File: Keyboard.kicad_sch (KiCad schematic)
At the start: 61 parts, among them SW1 SW_Push, SW10 SW_Push, SW11 SW_Push, SW12 SW_Push, SW13 SW_Push, SW14 SW_Push, SW15 SW_Push, SW16 SW_Push, SW17 SW_Push, SW18 SW_Push, SW19 SW_Push, SW2 SW_Push, SW20 SW_Push, SW3 SW_Push, SW4 SW_Push, SW5 SW_Push, SW6 SW_Push, SW7 SW_Push, SW8 SW_Push, SW9 SW_Push, U1 XIAO-nRF52840-SMD, U2 MCP23017_ML

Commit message: One last step before finalizing the KeyPad
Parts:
- SW1, SW10, SW11, SW12, SW13, SW14, SW15, SW16, SW17, SW18, SW19, SW2, SW20, SW3, SW4, SW5, SW6, SW7, SW8, SW9: footprint PCM_marbastlib-xp-choc:SW_choc_v2_HS_CPG135001S30_1u -> PCM_marbastlib-choc:SW_choc_v1_HS_CPG135001S30_1u
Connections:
- net BT_PIN: now also U1.2 (P0.03_A1_D1); no longer U1.1 (P0.02_A0_D0)
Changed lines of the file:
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@@
 	)
 	(no_connect
-		(at 143.51 55.88)
+		(at 143.51 52.07)
 	)
 	(no_connect
@@
 	(global_label "BT_PIN"
 		(shape input)
-		(at 143.51 52.07 180)
+		(at 143.51 55.88 180)
 		(fields_autoplaced yes)
 		(effects
@@
 		)
 		(property "Intersheetrefs" "${INTERSHEET_REFS}"
-			(at 133.6383 52.07 0)
+			(at 133.6383 55.88 0)
 			(effects
 				(font
@@
 			)
 		)
-		(property "Footprint" "PCM_marbastlib-xp-choc:SW_choc_v2_HS_CPG135001S30_1u"
+		(property "Footprint" "PCM_marbastlib-choc:SW_choc_v1_HS_CPG135001S30_1u"
 			(at 69.85 121.92 0)
 			(effects
@@
 			)
 		)
-		(property "Footprint" "PCM_marbastlib-xp-choc:SW_choc_v2_HS_CPG135001S30_1u"
+		(property "Footprint" "PCM_marbastlib-choc:SW_choc_v1_HS_CPG135001S30_1u"
 			(at 107.95 63.5 0)
 			(effects
@@
 			)
 		)
-		(property "Footprint" "PCM_marbastlib-xp-choc:SW_choc_v2_HS_CPG135001S30_1u"
+		(property "Footprint" "PCM_marbastlib-choc:SW_choc_v1_HS_CPG135001S30_1u"
 			(at 52.07 101.6 0)
 			(effects
@@
 			)
 		)
-		(property "Footprint" "PCM_marbastlib-xp-choc:SW_choc_v2_HS_CPG135001S30_1u"
+		(property "Footprint" "PCM_marbastlib-choc:SW_choc_v1_HS_CPG135001S30_1u"
 			(at 69.85 44.45 0)
 			(effects
@@
 			)
 		)
-		(property "Footprint" "PCM_marbastlib-xp-choc:SW_choc_v2_HS_CPG135001S30_1u"
+		(property "Footprint" "PCM_marbastlib-choc:SW_choc_v1_HS_CPG135001S30_1u"
 			(at 69.85 101.6 0)
 			(effects
@@
 			)
 		)
-		(property "Footprint" "PCM_marbastlib-xp-choc:SW_choc_v2_HS_CPG135001S30_1u"
+		(property "Footprint" "PCM_marbastlib-choc:SW_choc_v1_HS_CPG135001S30_1u"
 			(at 69.85 63.5 0)
 			(effects
@@
 			)
 		)
-		(property "Footprint" "PCM_marbastlib-xp-choc:SW_choc_v2_HS_CPG135001S30_1u"
+		(property "Footprint" "PCM_marbastlib-choc:SW_choc_v1_HS_CPG135001S30_1u"
 			(at 52.07 63.5 0)
 			(effects
@@
 			)
 		)
-		(property "Footprint" "PCM_marbastlib-xp-choc:SW_choc_v2_HS_CPG135001S30_1u"
+		(property "Footprint" "PCM_marbastlib-choc:SW_choc_v1_HS_CPG135001S30_1u"
 			(at 69.85 82.55 0)
 			(effects
@@
 			)
 		)
-		(property "Footprint" "PCM_marbastlib-xp-choc:SW_choc_v2_HS_CPG135001S30_1u"
+		(property "Footprint" "PCM_marbastlib-choc:SW_choc_v1_HS_CPG135001S30_1u"
 			(at 52.07 121.92 0)
 			(effects
@@
 			)
 		)
-		(property "Footprint" "PCM_marbastlib-xp-choc:SW_choc_v2_HS_CPG135001S30_1u"
+		(property "Footprint" "PCM_marbastlib-choc:SW_choc_v1_HS_CPG135001S30_1u"
 			(at 107.95 121.92 0)
 			(effects
@@
 			)
 		)
-		(property "Footprint" "PCM_marbastlib-xp-choc:SW_choc_v2_HS_CPG135001S30_1u"
+		(property "Footprint" "PCM_marbastlib-choc:SW_choc_v1_HS_CPG135001S30_1u"
 			(at 88.9 63.5 0)
 			(effects
@@
 			)
 		)
-		(property "Footprint" "PCM_marbastlib-xp-choc:SW_choc_v2_HS_CPG135001S30_1u"
+		(property "Footprint" "PCM_marbastlib-choc:SW_choc_v1_HS_CPG135001S30_1u"
 			(at 88.9 121.92 0)
 			(effects
@@
 			)
 		)
-		(property "Footprint" "PCM_marbastlib-xp-choc:SW_choc_v2_HS_CPG135001S30_1u"
+		(property "Footprint" "PCM_marbastlib-choc:SW_choc_v1_HS_CPG135001S30_1u"
 			(at 88.9 82.55 0)
 			(effects
@@
 			)
 		)
-		(property "Footprint" "PCM_marbastlib-xp-choc:SW_choc_v2_HS_CPG135001S30_1u"
+		(property "Footprint" "PCM_marbastlib-choc:SW_choc_v1_HS_CPG135001S30_1u"
 			(at 88.9 101.6 0)
 			(effects
@@
 			)
 		)
-		(property "Footprint" "PCM_marbastlib-xp-choc:SW_choc_v2_HS_CPG135001S30_1u"
+		(property "Footprint" "PCM_marbastlib-choc:SW_choc_v1_HS_CPG135001S30_1u"
 			(at 88.9 44.45 0)
 			(effects
@@
 			)
 		)
-		(property "Footprint" "PCM_marbastlib-xp-choc:SW_choc_v2_HS_CPG135001S30_1u"
+		(property "Footprint" "PCM_marbastlib-choc:SW_choc_v1_HS_CPG135001S30_1u"
 			(at 52.07 82.55 0)
 			(effects
@@
 			)
 		)
-		(property "Footprint" "PCM_marbastlib-xp-choc:SW_choc_v2_HS_CPG135001S30_1u"
+		(property "Footprint" "PCM_marbastlib-choc:SW_choc_v1_HS_CPG135001S30_1u"
 			(at 107.95 101.6 0)
 			(effects
@@
 			)
 		)
-		(property "Footprint" "PCM_marbastlib-xp-choc:SW_choc_v2_HS_CPG135001S30_1u"
+		(property "Footprint" "PCM_marbastlib-choc:SW_choc_v1_HS_CPG135001S30_1u"
 			(at 107.95 82.55 0)
 			(effects
@@
 			)
 		)
-		(property "Footprint" "PCM_marbastlib-xp-choc:SW_choc_v2_HS_CPG135001S30_1u"
+		(property "Footprint" "PCM_marbastlib-choc:SW_choc_v1_HS_CPG135001S30_1u"
 			(at 107.95 44.45 0)
 			(effects
@@
 			)
 		)
-		(property "Footprint" "PCM_marbastlib-xp-choc:SW_choc_v2_HS_CPG135001S30_1u"
+		(property "Footprint" "PCM_marbastlib-choc:SW_choc_v1_HS_CPG135001S30_1u"
 			(at 52.07 44.45 0)
 			(effects

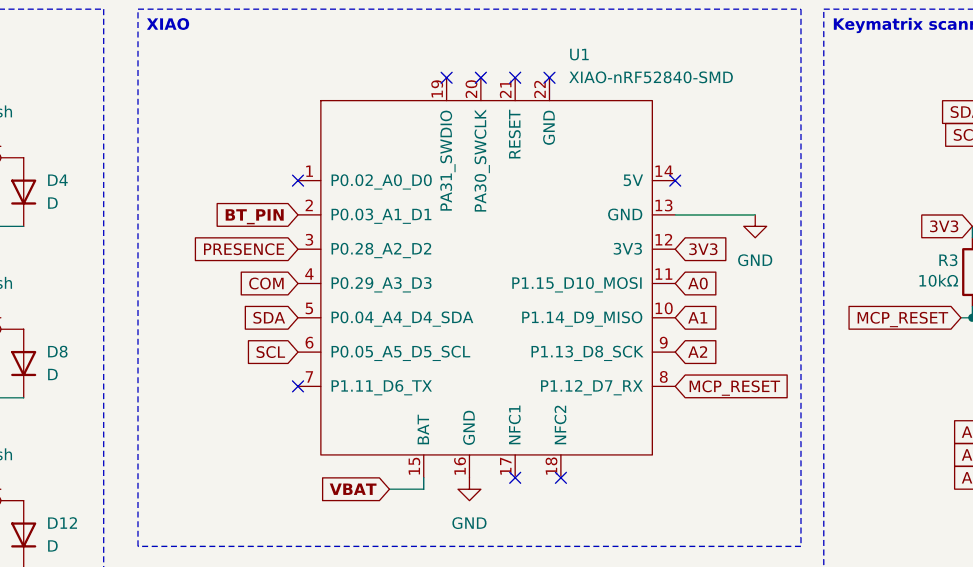
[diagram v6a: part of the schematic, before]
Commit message: Finalized the keypad
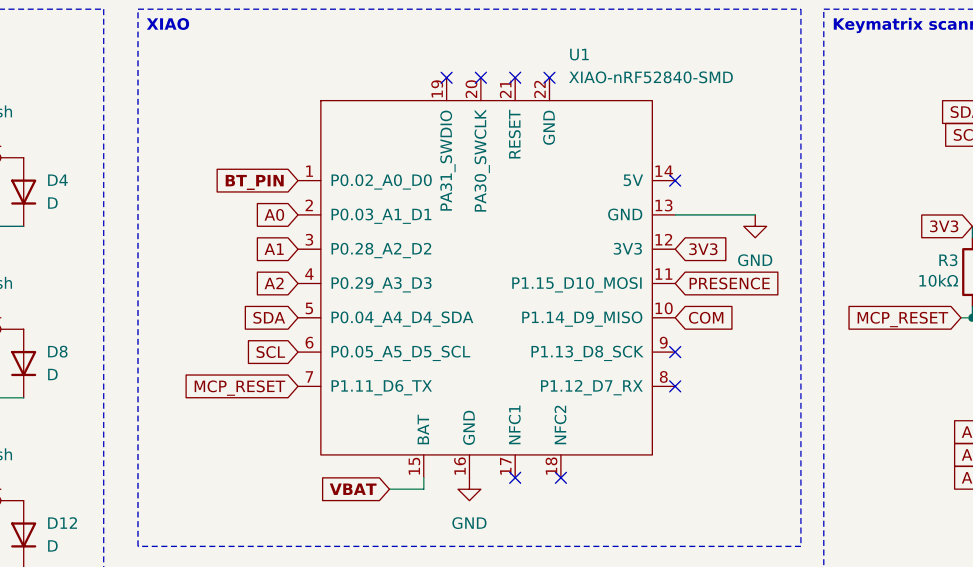
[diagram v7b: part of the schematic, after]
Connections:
- net A0: now also U1.2 (P0.03_A1_D1); no longer U1.11 (P1.15_D10_MOSI)
- net A1: now also U1.3 (P0.28_A2_D2); no longer U1.10 (P1.14_D9_MISO)
- net A2: now also U1.4 (P0.29_A3_D3); no longer U1.9 (P1.13_D8_SCK)
- net BT_PIN: now also U1.1 (P0.02_A0_D0); no longer U1.2 (P0.03_A1_D1)
- net COM: now also U1.10 (P1.14_D9_MISO); no longer U1.4 (P0.29_A3_D3)
- net MCP_RESET: now also U1.7 (P1.11_D6_TX); no longer U1.8 (P1.12_D7_RX)
- net PRESENCE: now also U1.11 (P1.15_D10_MOSI); no longer U1.3 (P0.28_A2_D2)

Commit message: Main board layout
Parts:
- removed D1, D10, D11, D12, D13, D14, D15, D16, D17, D18, D19, D2, D20, D3, D4, D5, D6, D7, D8, D9: D, Diode_SMD:D_SOD-123, symbol Device:D
- removed H1, H2, H3, H4, H5, H6: MountingHole, MountingHole:MountingHole_2.2mm_M2, symbol Mechanical:MountingHole
- removed R1: 806kΩ, Resistor_SMD:R_0805_2012Metric, symbol Device:R
- removed R2: 2MΩ, Resistor_SMD:R_0805_2012Metric, symbol Device:R
- removed R3: 10kΩ, Resistor_SMD:R_0805_2012Metric, symbol Device:R
- removed R4, R5: 4.7kΩ, Resistor_SMD:R_0805_2012Metric, symbol Device:R
- removed SW1, SW10, SW11, SW12, SW13, SW14, SW15, SW16, SW17, SW18, SW19, SW2, SW20, SW3, SW4, SW5, SW6, SW7, SW8, SW9: SW_Push, PCM_marbastlib-choc:SW_choc_v1_HS_CPG135001S30_1u, symbol Switch:SW_Push
- removed TP1: BAT, TestPoint:TestPoint_Pad_D2.0mm, symbol Connector:TestPoint
- removed TP2: GND, TestPoint:TestPoint_Pad_D2.0mm, symbol Connector:TestPoint
- removed TP3, TP4, TP5, TP6, TP7, TP8: TestPoint, TestPoint:TestPoint_Pad_D2.0mm, symbol Connector:TestPoint
- removed U1: XIAO-nRF52840-SMD, Seeed Studio XIAO Series Library:modified-XIAO-nRF52840-SMD, symbol Seeed_Studio_XIAO_Series:XIAO-nRF52840-SMD
- removed U2: MCP23017_ML, Package_DFN_QFN:QFN-28-1EP_6x6mm_P0.65mm_EP4.25x4.25mm, symbol Interface_Expansion:MCP23017_ML
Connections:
- no-connect marks 19 -> 0
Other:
- added sheet Keypad_module (Keypad_module.kicad_sch)
- added sheet Main_board (Main_board.kicad_sch)
